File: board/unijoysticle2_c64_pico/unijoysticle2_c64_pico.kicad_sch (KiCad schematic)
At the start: 0 parts

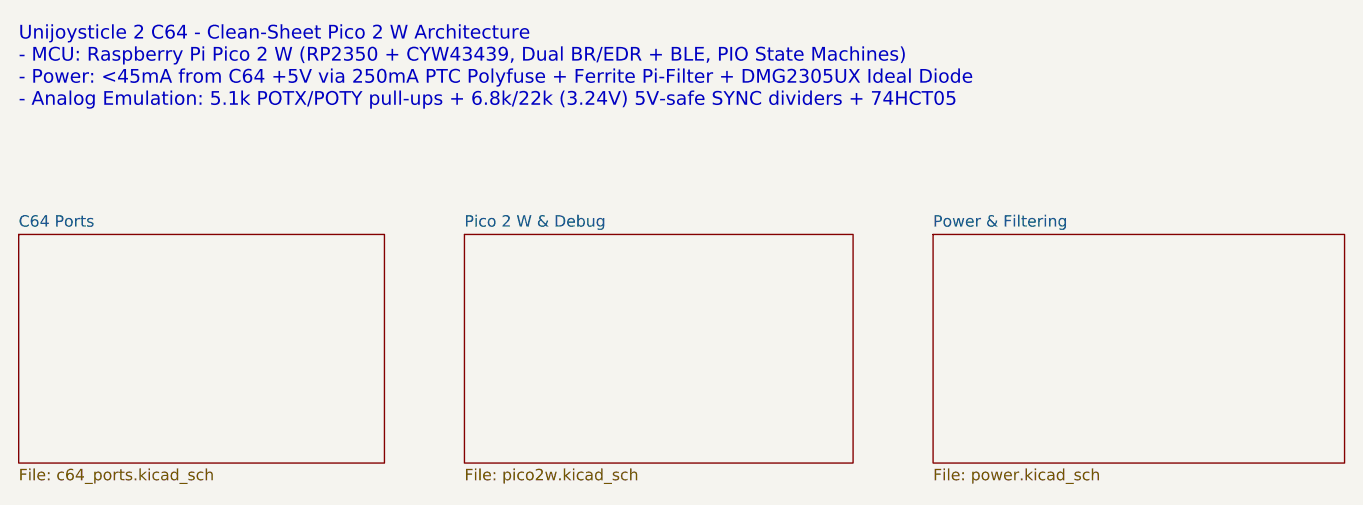
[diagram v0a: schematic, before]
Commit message: improved pico sid interrupt generation
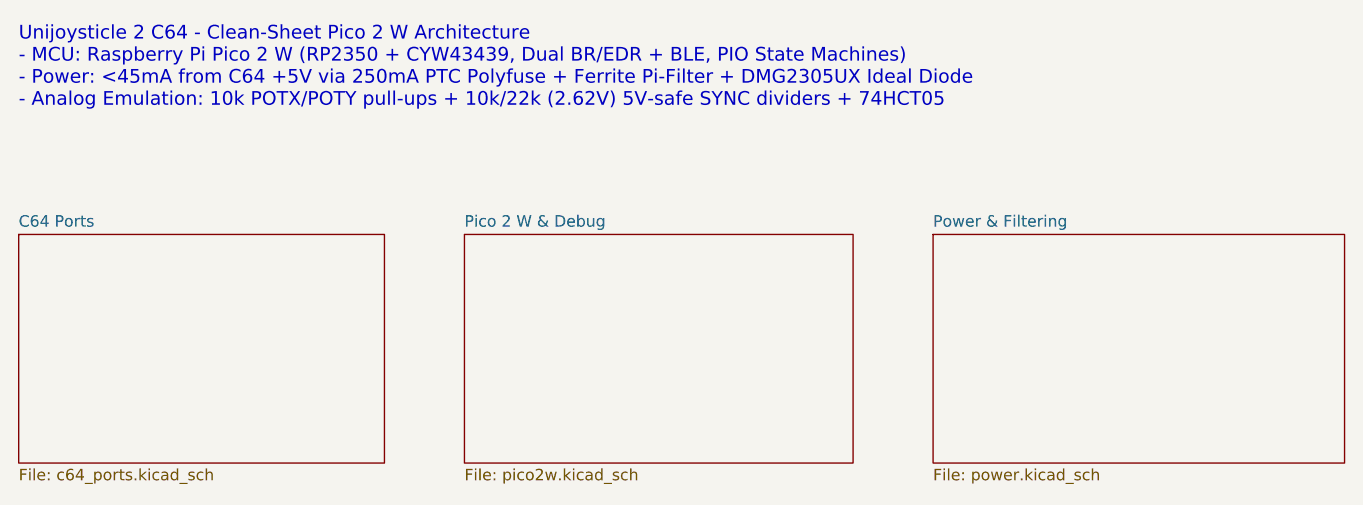
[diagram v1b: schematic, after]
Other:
- note added: "Unijoysticle 2 C64 - Clean-Sheet Pico 2 W Architecture - MCU: Raspberry Pi Pico 2 W (RP2350 + CYW43439, Dual BR/EDR + BLE, PIO State Machines) - Power: <45mA from C64 +5V via 250mA PTC Polyfuse + Ferrite Pi-Filter + DMG2305UX Ideal Diode - Analog Emulation: 10k POTX/POTY pull-ups + 10k/22k (2.62V) 5V-safe SYNC dividers + 74HCT05"
- note removed: "Unijoysticle 2 C64 - Clean-Sheet Pico 2 W Architecture - MCU: Raspberry Pi Pico 2 W (RP2350 + CYW43439, Dual BR/EDR + BLE, PIO State Machines) - Power: <45mA from C64 +5V via 250mA PTC Polyfuse + Ferrite Pi-Filter + DMG2305UX Ideal Diode - Analog Emulation: 5.1k POTX/POTY pull-ups + 6.8k/22k (3.24V) 5V-safe SYNC dividers + 74HCT05"
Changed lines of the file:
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@@
 		(comment 2 "Full C64 Joystick, 1351 Mouse, and 1311/1312 Paddle Emulation")
 	)
-	(text "Unijoysticle 2 C64 - Clean-Sheet Pico 2 W Architecture\n- MCU: Raspberry Pi Pico 2 W (RP2350 + CYW43439, Dual BR/EDR + BLE, PIO State Machines)\n- Power: <45mA from C64 +5V via 250mA PTC Polyfuse + Ferrite Pi-Filter + DMG2305UX Ideal Diode\n- Analog Emulation: 5.1k POTX/POTY pull-ups + 6.8k/22k (3.24V) 5V-safe SYNC dividers + 74HCT05"
+	(text "Unijoysticle 2 C64 - Clean-Sheet Pico 2 W Architecture\n- MCU: Raspberry Pi Pico 2 W (RP2350 + CYW43439, Dual BR/EDR + BLE, PIO State Machines)\n- Power: <45mA from C64 +5V via 250mA PTC Polyfuse + Ferrite Pi-Filter + DMG2305UX Ideal Diode\n- Analog Emulation: 10k POTX/POTY pull-ups + 10k/22k (2.62V) 5V-safe SYNC dividers + 74HCT05"
 		(exclude_from_sim no)
 		(at 62.23 48.26 0)
